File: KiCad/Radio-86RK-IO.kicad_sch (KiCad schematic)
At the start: 16 parts, among them J5 Serial, J6 Parallel, Q2 2N3904, U16 7486/К155ЛП5, U20 7400/К155ЛА3, U22 SN75154N/К170УП2В, U23 SN75150P/К170АП2, U24 SN75150P/К170АП2, U3 8251A/КР580ВВ51А, U4 8253/КР580ВИ53, U6 8255A/КР580ВВ55А

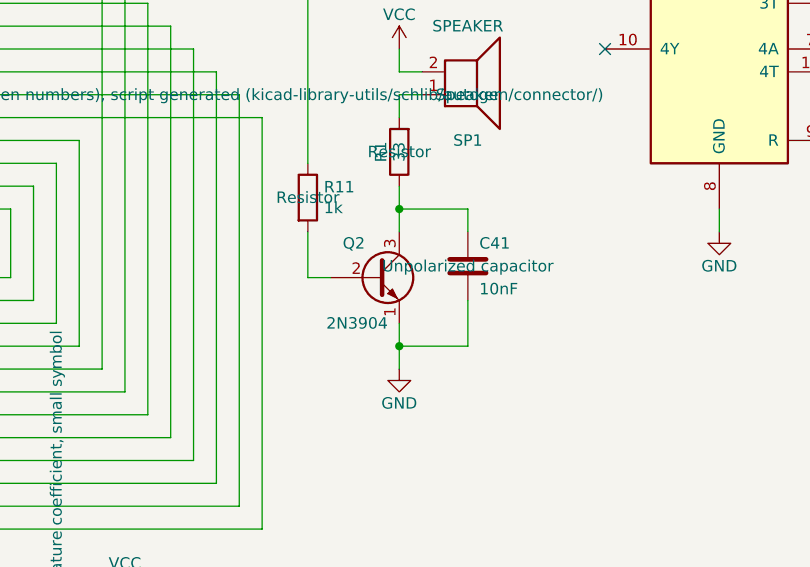
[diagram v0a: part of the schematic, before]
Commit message: Relink Q1/Q2 from stale Device:Q_NPN_EBC to Transistor_BJT:Q_NPN_EBC
The symbol moved libraries between KiCad versions (same name, same E/B/C
pinout) -- Device no longer carries it in KiCad 10. Resolves 2 ERC
lib_symbol_issues warnings. Also includes a mop-up Update Symbol from
Library pass to clear an incidental lib_symbol_mismatch regression the
relink introduced on U19/U20's cached copies in the same files (metadata-
only, Datasheet/Description fields, no connectivity impact).

Co-Authored-By: Claude Sonnet 5 <noreply@anthropic.com>
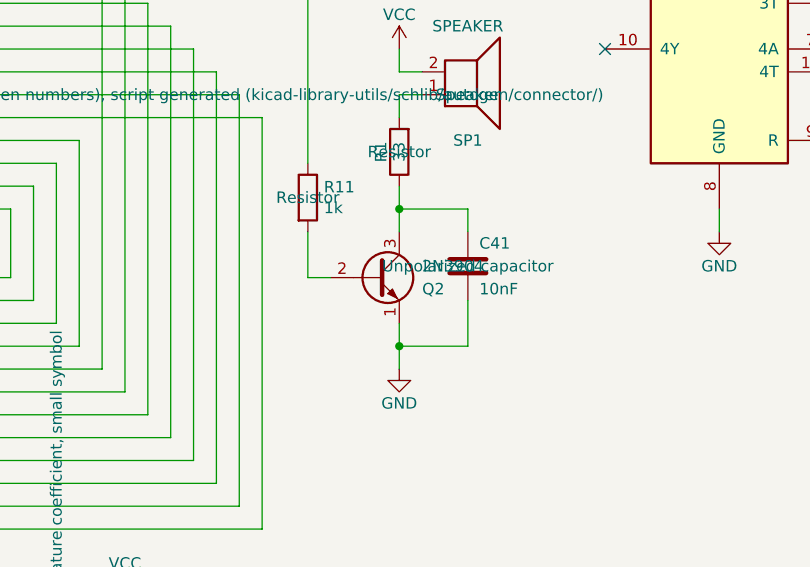
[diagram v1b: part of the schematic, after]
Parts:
- removed Q2: 2N3904, Package_TO_SOT_THT:TO-92_Inline_Wide, symbol Device:Q_NPN_EBC
- added Q2: 2N3904, Package_TO_SOT_THT:TO-92_Inline_Wide, symbol Transistor_BJT:Q_NPN_EBC
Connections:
- net GND: now also Q2.1 (E)
- net at R11.2: now also Q2.2 (B)
- net at C41.1, R1.1: now also Q2.3 (C)
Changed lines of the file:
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@@
-	)
-	(symbol
-		(lib_id "Device:Q_NPN_EBC")
-		(at 170.18 154.94 0)
-		(unit 1)
-		(body_style 1)
-		(exclude_from_sim no)
-		(in_bom yes)
-		(on_board yes)
-		(in_pos_files yes)
-		(dnp no)
-		(property "Reference" "Q2"
-			(at 168.91 151.13 0)
-			(show_name no)
-			(do_not_autoplace no)
-			(effects
-				(font
-					(size 1.27 1.27)
-				)
-				(justify right)
-			)
-		)
-		(property "Value" "2N3904"
-			(at 171.45 160.02 0)
-			(show_name no)
-			(do_not_autoplace no)
-			(effects
-				(font
-					(size 1.27 1.27)
-				)
-				(justify right)
-			)
-		)
-		(property "Footprint" "Package_TO_SOT_THT:TO-92_Inline_Wide"
-			(at 175.26 152.4 0)
-			(hide yes)
-			(show_name no)
-			(do_not_autoplace no)
-			(effects
-				(font
-					(size 1.27 1.27)
-				)
-			)
-		)
-		(property "Datasheet" ""
-			(at 170.18 154.94 0)
-			(show_name no)
-			(do_not_autoplace no)
-			(effects
-				(font
-					(size 1.27 1.27)
-				)
-			)
-		)
-		(property "Description" ""
-			(at 170.18 154.94 0)
-			(show_name no)
-			(do_not_autoplace no)
-			(effects
-				(font
-					(size 1.27 1.27)
-				)
-			)
-		)
-		(pin "1"
-		)
-		(pin "2"
-		)
-		(pin "3"
-		)
-		(instances
-			(project "Radio-86RK"
-				(path "/8e697b96-cf4c-43ef-b321-8c2422b088bf/00000000-0000-0000-0000-00006434046a"
-					(reference "Q2")
-					(unit 1)
-				)
-			)
-		)
 	)
 	(symbol
@@
 				)
 			)
+		)
+	)
+	(symbol
+		(lib_id "Transistor_BJT:Q_NPN_EBC")
+		(at 170.18 154.94 0)
+		(unit 1)
+		(body_style 1)
+		(exclude_from_sim no)
+		(in_bom yes)
+		(on_board yes)
+		(in_pos_files yes)
+		(dnp no)
+		(property "Reference" "Q2"
+			(at 175.26 156.21 0)
+			(show_name no)
+			(do_not_autoplace no)
+			(effects
+				(font
+					(size 1.27 1.27)
+				)
+				(justify left)
+			)
+		)
+		(property "Value" "2N3904"
+			(at 175.26 153.67 0)
+			(show_name no)
+			(do_not_autoplace no)
+			(effects
+				(font
+					(size 1.27 1.27)
+				)
+				(justify left)
+			)
+		)
+		(property "Footprint" "Package_TO_SOT_THT:TO-92_Inline_Wide"
+			(at 175.26 157.48 0)
+			(hide yes)
+			(show_name no)
+			(do_not_autoplace no)
+			(effects
+				(font
+					(size 1.27 1.27)
+				)
+			)
+		)
+		(property "Datasheet" ""
+			(at 170.18 154.94 0)
+			(hide yes)
+			(show_name no)
+			(do_not_autoplace no)
+			(effects
+				(font
+					(size 1.27 1.27)
+				)
+			)
+		)
+		(property "Description" "NPN transistor, emitter/base/collector"
+			(at 170.18 154.94 0)
+			(hide yes)
+			(show_name no)
+			(do_not_autoplace no)
+			(effects
+				(font
+					(size 1.27 1.27)
+				)
+			)
+		)
+		(property "Sim.Device" "NPN"
+			(at 170.18 154.94 0)
+			(hide yes)
+			(show_name no)
+			(do_not_autoplace no)
+			(effects
+				(font
+					(size 1.27 1.27)
+				)
+			)
+		)
+		(property "Sim.Pins" "1=E 2=B 3=C"
+			(at 170.18 154.94 0)
+			(hide yes)
+			(show_name no)
+			(do_not_autoplace no)
+			(effects
+				(font
+					(size 1.27 1.27)
+				)
+			)
+		)
+		(pin "1"
+		)
+		(pin "2"
+		)
+		(pin "3"
+		)
+		(instances
+			(project "Radio-86RK"
+				(path "/8e697b96-cf4c-43ef-b321-8c2422b088bf/00000000-0000-0000-0000-00006434046a"
+					(reference "Q2")
+					(unit 1)
+				)
+			)
